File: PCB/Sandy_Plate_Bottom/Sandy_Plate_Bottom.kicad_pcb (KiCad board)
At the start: 2 copper layers, 285 x 94.6 mm, 32 parts

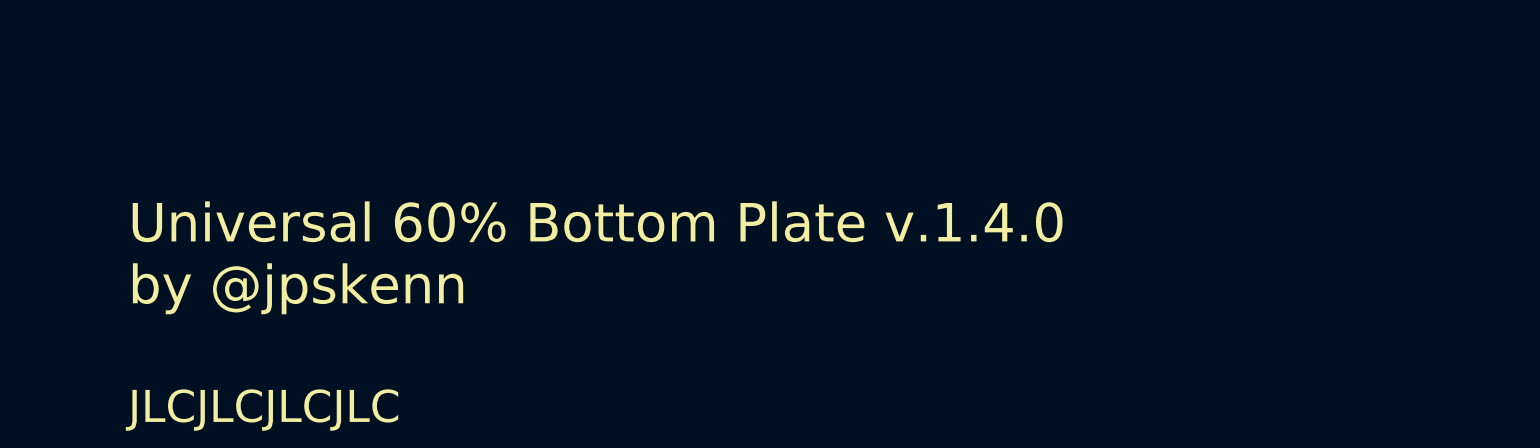
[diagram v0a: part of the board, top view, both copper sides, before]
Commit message: ネジ穴まわりのクリアランスを調整
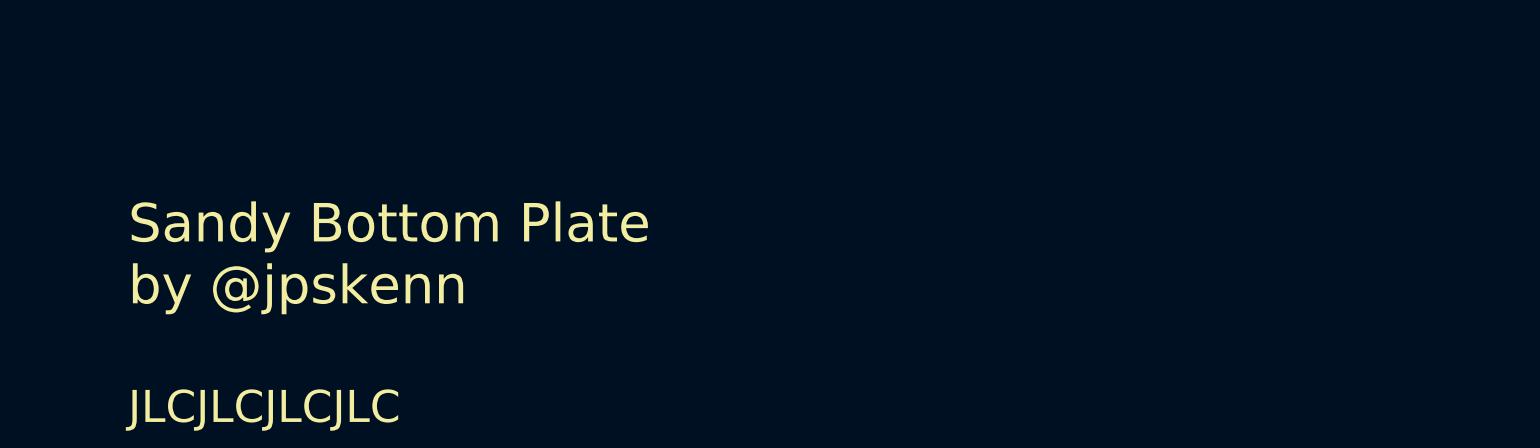
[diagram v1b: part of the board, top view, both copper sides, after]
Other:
- board text added: "Sandy Bottom Plate by @jpskenn"
- board text removed: "Universal 60% Bottom Plate v.1.4.0 by @jpskenn"
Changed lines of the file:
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@@
 			(size 2.9 2.4)
 			(drill oval 2.9 2.4)
-			(layers "*.Cu" "*.Mask")
+			(layers "F&B.Cu" "*.Mask")
+			(clearance 1.5)
 		)
 		(pad "" np_thru_hole circle
@@
 			(size 2.4994 2.4994)
 			(drill 2.4994)
-			(layers "*.Cu" "*.Mask")
+			(layers "F&B.Cu" "*.Mask")
+			(clearance 1.5)
 		)
 		(pad "" np_thru_hole oval
@@
 			(size 5.2 2.4)
 			(drill oval 5.2 2.4)
-			(layers "*.Cu" "*.Mask")
+			(layers "F&B.Cu" "*.Mask")
+			(clearance 1.5)
 		)
 		(pad "" np_thru_hole oval
@@
 			(size 2.9 2.4)
 			(drill oval 2.9 2.4)
-			(layers "*.Cu" "*.Mask")
+			(layers "F&B.Cu" "*.Mask")
+			(clearance 1.5)
 		)
 	)
@@
 		(layer "Eco1.User")
 	)
-	(gr_text "Universal 60% Bottom Plate v.1.4.0\nby @jpskenn"
+	(gr_text "Sandy Bottom Plate\nby @jpskenn"
 		(at 70.246875 66.675 0)
 		(layer "F.SilkS")
@@
 	)
 	(zone
-		(net 0)
-		(net_name "")
-		(layer "F.Cu")
-		(hatch edge 0.508)
-		(connect_pads
-			(clearance 0)
-		)
-		(min_thickness 0.254)
-		(filled_areas_thickness no)
-		(keepout
-			(tracks not_allowed)
-			(vias allowed)
-			(pads allowed)
-			(copperpour not_allowed)
-			(footprints allowed)
-		)
-		(fill
-			(thermal_gap 0.508)
-			(thermal_bridge_width 0.508)
-		)
-		(polygon
-			(pts
-				(xy 301.4346 70.87704) (xy 301.4346 76.26184) (xy 296.8626 76.26184) (xy 296.8626 70.87704)
-			)
-		)
-	)
-	(zone
-		(net 0)
-		(net_name "")
-		(layer "F.Cu")
-		(hatch edge 0.508)
-		(connect_pads
-			(clearance 0)
-		)
-		(min_thickness 0.254)
-		(filled_areas_thickness no)
-		(keepout
-			(tracks not_allowed)
-			(vias allowed)
-			(pads allowed)
-			(copperpour not_allowed)
-			(footprints allowed)
-		)
-		(fill
-			(thermal_gap 0.508)
-			(thermal_bridge_width 0.508)
-		)
-		(polygon
-			(pts
-				(xy 19.0374 70.87704) (xy 19.0374 76.27224) (xy 14.4654 76.27224) (xy 14.4654 70.87704)
-			)
-		)
-	)
-	(zone
